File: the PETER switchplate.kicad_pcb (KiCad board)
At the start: 2 copper layers, 243.4 x 95.4 mm, 7 parts

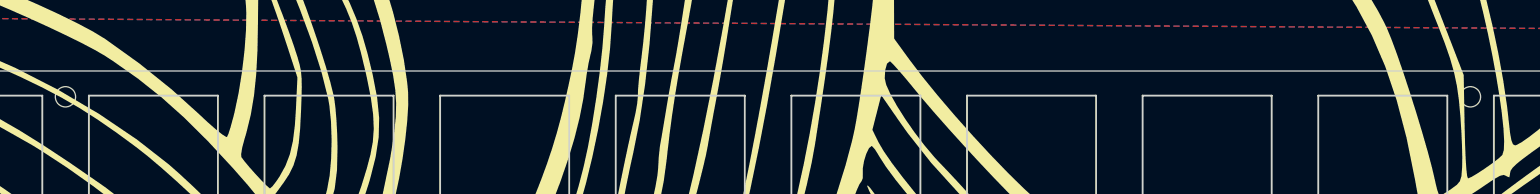
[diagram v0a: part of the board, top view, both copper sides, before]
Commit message: changes to pcb, plate, DRC cleanup
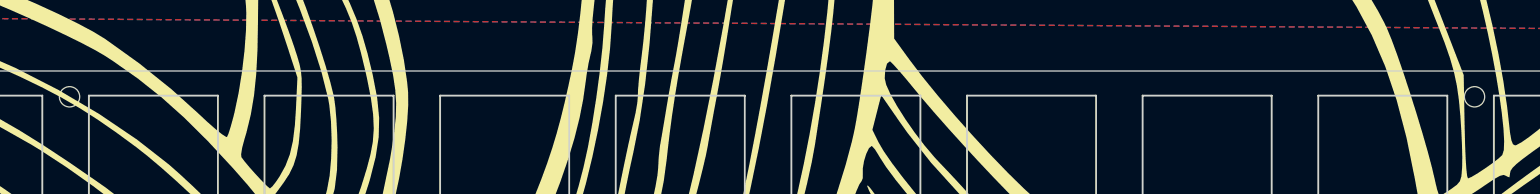
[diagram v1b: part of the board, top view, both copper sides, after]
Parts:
- moved H1 0.44 mm to (68.7, 49.8)
- moved H2 0.44 mm to (221.1, 49.8)
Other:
- board text removed: "add standoffs for stability?"
- board text removed: "add the pcb cut outs for bottom mounting"
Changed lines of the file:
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@@
   )
   (footprint "MountingHole:MountingHole_2.2mm_M2" (layer "F.Cu")
-    (at 68.2625 49.784)
+    (at 68.707 49.783999)
     (descr "Mounting Hole 2.2mm, no annular, M2")
     (tags "mounting hole 2.2mm no annular m2")
@@
   )
   (footprint "MountingHole:MountingHole_2.2mm_M2" (layer "F.Cu")
-    (at 220.6625 49.784)
+    (at 221.107 49.784)
     (descr "Mounting Hole 2.2mm, no annular, M2")
     (tags "mounting hole 2.2mm no annular m2")
@@
   (gr_line (start 41.94 63.657) (end 41.94 49.657) (layer "Edge.Cuts") (width 0.2))
   (gr_line (start 172.90875 139.857) (end 172.90875 125.857) (layer "Edge.Cuts") (width 0.2))
-  (gr_text "add standoffs for stability?" (at 165.481 41.402) (layer "F.Adhes")
-    (effects (font (size 1 1) (thickness 0.15)))
-  )
-  (gr_text "add standoffs for stability?" (at 95.377 151.638) (layer "F.Adhes")
-    (effects (font (size 1 1) (thickness 0.15)))
-  )
-  (gr_text "add standoffs for stability?" (at 186.944 149.987) (layer "F.Adhes")
-    (effects (font (size 1 1) (thickness 0.15)))
-  )
-  (gr_text "add the pcb cut outs for bottom mounting\n" (at 69.215 43.815) (layer "F.Adhes")
-    (effects (font (size 1 1) (thickness 0.15)))
-  )
-  (gr_text "add standoffs for stability?" (at 122.809 42.291) (layer "F.Adhes")
-    (effects (font (size 1 1) (thickness 0.15)))
-  )
   (gr_text "the PETER\n" (at 27.024694 101.6 -90) (layer "F.SilkS")
     (effects (font (size 2 2) (thickness 0.15)))
